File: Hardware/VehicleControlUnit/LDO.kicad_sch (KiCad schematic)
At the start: 5 parts, among them U1 MCP1826S

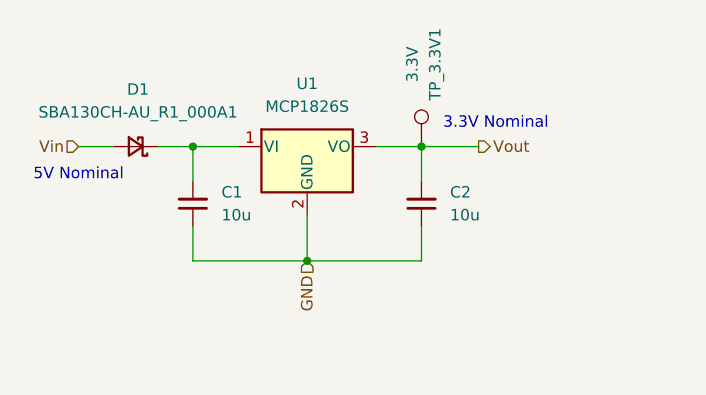
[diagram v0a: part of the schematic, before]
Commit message: mcu pinouts todo - peripherals done
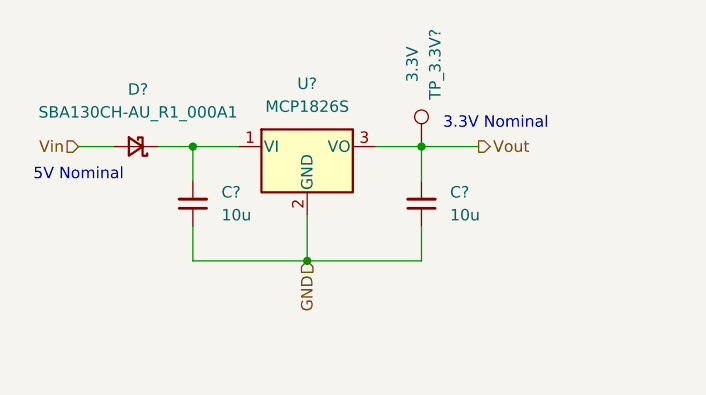
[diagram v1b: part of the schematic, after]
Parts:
- renumbered C2 to C?, C1 to C?, D1 to D?, TP_3.3V1 to TP_3.3V?, U1 to U?
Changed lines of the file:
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@@
 		(dnp no)
 		(fields_autoplaced yes)
-		(property "Reference" "C2"
+		(property "Reference" "C?"
 			(at 168.275 68.5735 0)
 			(show_name no)
@@
 		)
 		(instances
-			(project "LDO"
-				(path "/8ff43370-8d10-4d2c-b1a3-81d1c2934a98"
-					(reference "C2")
-					(unit 1)
-				)
-			)
-			(project "LeaderSOMBreakout"
-				(path "/e5b32072-3e3d-42a6-9d41-1a76d538e329/f3053c74-1ac6-4a33-80f3-565e8c4c2c7d"
+			(project "VehicleControlUnit"
+				(path "/e864fac9-3897-46c9-9101-6d5488c6cd3a/f16a8bc3-f058-4d27-badd-0afc148d009e/da76194f-59e6-4b82-959b-538a81e9eb86"
 					(reference "C?")
-					(unit 1)
-				)
-			)
-			(project "VehicleControlUnit"
-				(path "/e864fac9-3897-46c9-9101-6d5488c6cd3a/3025f6f3-aa95-4f38-bd50-766a08164531"
-					(reference "C2")
 					(unit 1)
 				)
@@
 		(in_pos_files yes)
 		(dnp no)
-		(property "Reference" "TP_3.3V1"
+		(property "Reference" "TP_3.3V?"
 			(at 166.624 54.356 90)
 			(show_name no)
@@
 		)
 		(instances
-			(project "LDO"
-				(path "/8ff43370-8d10-4d2c-b1a3-81d1c2934a98"
-					(reference "TP_3.3V1")
-					(unit 1)
-				)
-			)
 			(project "VehicleControlUnit"
-				(path "/e864fac9-3897-46c9-9101-6d5488c6cd3a/3025f6f3-aa95-4f38-bd50-766a08164531"
-					(reference "TP_3.3V1")
+				(path "/e864fac9-3897-46c9-9101-6d5488c6cd3a/f16a8bc3-f058-4d27-badd-0afc148d009e/da76194f-59e6-4b82-959b-538a81e9eb86"
+					(reference "TP_3.3V?")
 					(unit 1)
 				)
@@
 		(dnp no)
 		(fields_autoplaced yes)
-		(property "Reference" "U1"
+		(property "Reference" "U?"
 			(at 152.4 56.515 0)
 			(show_name no)
@@
 		)
 		(instances
-			(project ""
-				(path "/8ff43370-8d10-4d2c-b1a3-81d1c2934a98"
-					(reference "U1")
-					(unit 1)
-				)
-			)
 			(project "VehicleControlUnit"
-				(path "/e864fac9-3897-46c9-9101-6d5488c6cd3a/3025f6f3-aa95-4f38-bd50-766a08164531"
-					(reference "U1")
+				(path "/e864fac9-3897-46c9-9101-6d5488c6cd3a/f16a8bc3-f058-4d27-badd-0afc148d009e/da76194f-59e6-4b82-959b-538a81e9eb86"
+					(reference "U?")
 					(unit 1)
 				)
@@
 		(dnp no)
 		(fields_autoplaced yes)
-		(property "Reference" "D1"
+		(property "Reference" "D?"
 			(at 133.604 57.15 0)
 			(show_name no)
@@
 		)
 		(instances
-			(project ""
-				(path "/8ff43370-8d10-4d2c-b1a3-81d1c2934a98"
-					(reference "D1")
-					(unit 1)
-				)
-			)
 			(project "VehicleControlUnit"
-				(path "/e864fac9-3897-46c9-9101-6d5488c6cd3a/3025f6f3-aa95-4f38-bd50-766a08164531"
-					(reference "D1")
+				(path "/e864fac9-3897-46c9-9101-6d5488c6cd3a/f16a8bc3-f058-4d27-badd-0afc148d009e/da76194f-59e6-4b82-959b-538a81e9eb86"
+					(reference "D?")
 					(unit 1)
 				)
@@
 		(dnp no)
 		(fields_autoplaced yes)
-		(property "Reference" "C1"
+		(property "Reference" "C?"
 			(at 142.875 68.5735 0)
 			(show_name no)
@@
 		)
 		(instances
-			(project "LDO"
-				(path "/8ff43370-8d10-4d2c-b1a3-81d1c2934a98"
-					(reference "C1")
-					(unit 1)
-				)
-			)
-			(project ""
-				(path "/e5b32072-3e3d-42a6-9d41-1a76d538e329/f3053c74-1ac6-4a33-80f3-565e8c4c2c7d"
+			(project "VehicleControlUnit"
+				(path "/e864fac9-3897-46c9-9101-6d5488c6cd3a/f16a8bc3-f058-4d27-badd-0afc148d009e/da76194f-59e6-4b82-959b-538a81e9eb86"
 					(reference "C?")
 					(unit 1)
 				)
-			)
-			(project "VehicleControlUnit"
-				(path "/e864fac9-3897-46c9-9101-6d5488c6cd3a/3025f6f3-aa95-4f38-bd50-766a08164531"
-					(reference "C1")
-					(unit 1)
-				)

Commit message: VCU more like diddle-u, mika time
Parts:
- gave numbers to parts that had none: 5
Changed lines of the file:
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@@
+		(color 0 0 0 0)
+	)
+	(junction
+		(at 142.24 63.5)
+		(diameter 0)
 		(color 0 0 0 0)
 	)
@@
 	(wire
 		(pts
-			(xy 139.7 63.5) (xy 144.78 63.5)
+			(xy 139.7 63.5) (xy 142.24 63.5)
 		)
 		(stroke
@@
 		(pts
 			(xy 165.1 63.5) (xy 171.45 63.5)
+		)
+		(stroke
+			(width 0)
+			(type default)
+		)
+	)
+	(wire
+		(pts
+			(xy 142.24 63.5) (xy 144.78 63.5)
 		)
 		(stroke
@@
 		(dnp no)
 		(fields_autoplaced yes)
-		(property "Reference" "C?"
+		(property "Reference" "C6"
 			(at 168.275 68.5735 0)
 			(show_name no)
@@
 			(project "VehicleControlUnit"
 				(path "/e864fac9-3897-46c9-9101-6d5488c6cd3a/f16a8bc3-f058-4d27-badd-0afc148d009e/da76194f-59e6-4b82-959b-538a81e9eb86"
-					(reference "C?")
+					(reference "C6")
 					(unit 1)
 				)
@@
 		(in_pos_files yes)
 		(dnp no)
-		(property "Reference" "TP_3.3V?"
+		(property "Reference" "TP_3.3V1"
 			(at 166.624 54.356 90)
 			(show_name no)
@@
 			(project "VehicleControlUnit"
 				(path "/e864fac9-3897-46c9-9101-6d5488c6cd3a/f16a8bc3-f058-4d27-badd-0afc148d009e/da76194f-59e6-4b82-959b-538a81e9eb86"
-					(reference "TP_3.3V?")
+					(reference "TP_3.3V1")
 					(unit 1)
 				)
@@
 		(dnp no)
 		(fields_autoplaced yes)
-		(property "Reference" "U?"
+		(property "Reference" "U2"
 			(at 152.4 56.515 0)
 			(show_name no)
@@
 			(project "VehicleControlUnit"
 				(path "/e864fac9-3897-46c9-9101-6d5488c6cd3a/f16a8bc3-f058-4d27-badd-0afc148d009e/da76194f-59e6-4b82-959b-538a81e9eb86"
-					(reference "U?")
+					(reference "U2")
 					(unit 1)
 				)
@@
 		(dnp no)
 		(fields_autoplaced yes)
-		(property "Reference" "D?"
+		(property "Reference" "D1"
 			(at 133.604 57.15 0)
 			(show_name no)
@@
 			(project "VehicleControlUnit"
 				(path "/e864fac9-3897-46c9-9101-6d5488c6cd3a/f16a8bc3-f058-4d27-badd-0afc148d009e/da76194f-59e6-4b82-959b-538a81e9eb86"
-					(reference "D?")
+					(reference "D1")
+					(unit 1)
+				)
+			)
+		)
+	)
+	(symbol
+		(lib_id "power:PWR_FLAG")
+		(at 142.24 63.5 180)
+		(unit 1)
+		(body_style 1)
+		(exclude_from_sim no)
+		(in_bom yes)
+		(on_board yes)
+		(in_pos_files yes)
+		(dnp no)
+		(fields_autoplaced yes)
+		(property "Reference" "#FLG04"
+			(at 142.24 65.405 0)
+			(hide yes)
+			(show_name no)
+			(do_not_autoplace no)
+			(effects
+				(font
+					(size 1.27 1.27)
+				)
+			)
+		)
+		(property "Value" "PWR_FLAG"
+			(at 142.24 68.58 0)
+			(hide yes)
+			(show_name no)
+			(do_not_autoplace no)
+			(effects
+				(font
+					(size 1.27 1.27)
+				)
+			)
+		)
+		(property "Footprint" ""
+			(at 142.24 63.5 0)
+			(hide yes)
+			(show_name no)
+			(do_not_autoplace no)
+			(effects
+				(font
+					(size 1.27 1.27)
+				)
+			)
+		)
+		(property "Datasheet" ""
+			(at 142.24 63.5 0)
+			(hide yes)
+			(show_name no)
+			(do_not_autoplace no)
+			(effects
+				(font
+					(size 1.27 1.27)
+				)
+			)
+		)
+		(property "Description" "Special symbol for telling ERC where power comes from"
+			(at 142.24 63.5 0)
+			(hide yes)
+			(show_name no)
+			(do_not_autoplace no)
+			(effects
+				(font
+					(size 1.27 1.27)
+				)
+			)
+		)
+		(pin "1"
+		)
+		(instances
+			(project "VehicleControlUnit"
+				(path "/e864fac9-3897-46c9-9101-6d5488c6cd3a/f16a8bc3-f058-4d27-badd-0afc148d009e/da76194f-59e6-4b82-959b-538a81e9eb86"
+					(reference "#FLG04")
 					(unit 1)
 				)
@@
 		(dnp no)
 		(fields_autoplaced yes)
-		(property "Reference" "C?"
+		(property "Reference" "C5"
 			(at 142.875 68.5735 0)
 			(show_name no)
@@
 			(project "VehicleControlUnit"
 				(path "/e864fac9-3897-46c9-9101-6d5488c6cd3a/f16a8bc3-f058-4d27-badd-0afc148d009e/da76194f-59e6-4b82-959b-538a81e9eb86"
-					(reference "C?")
+					(reference "C5")
 					(unit 1)
 				)

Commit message: pre layout
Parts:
- renumbered C5 to C18, C6 to C19, D1 to D3, U2 to U3
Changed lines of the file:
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@@
-		(color 0 0 0 0)
-	)
-	(junction
-		(at 142.24 63.5)
-		(diameter 0)
 		(color 0 0 0 0)
 	)
@@
 	(wire
 		(pts
-			(xy 139.7 63.5) (xy 142.24 63.5)
+			(xy 139.7 63.5) (xy 144.78 63.5)
 		)
 		(stroke
@@
 		(pts
 			(xy 165.1 63.5) (xy 171.45 63.5)
-		)
-		(stroke
-			(width 0)
-			(type default)
-		)
-	)
-	(wire
-		(pts
-			(xy 142.24 63.5) (xy 144.78 63.5)
 		)
 		(stroke
@@
 		(dnp no)
 		(fields_autoplaced yes)
-		(property "Reference" "C6"
+		(property "Reference" "C19"
 			(at 168.275 68.5735 0)
 			(show_name no)
@@
 		)
 		(instances
+			(project "LDO"
+				(path "/8ff43370-8d10-4d2c-b1a3-81d1c2934a98"
+					(reference "C2")
+					(unit 1)
+				)
+			)
+			(project "LeaderSOMBreakout"
+				(path "/e5b32072-3e3d-42a6-9d41-1a76d538e329/f3053c74-1ac6-4a33-80f3-565e8c4c2c7d"
+					(reference "C?")
+					(unit 1)
+				)
+			)
 			(project "VehicleControlUnit"
-				(path "/e864fac9-3897-46c9-9101-6d5488c6cd3a/f16a8bc3-f058-4d27-badd-0afc148d009e/da76194f-59e6-4b82-959b-538a81e9eb86"
-					(reference "C6")
+				(path "/e864fac9-3897-46c9-9101-6d5488c6cd3a/f16a8bc3-f058-4d27-badd-0afc148d009e/853b16d2-2efa-4055-8a9a-ea208220d84d"
+					(reference "C19")
 					(unit 1)
 				)
@@
 		)
 		(instances
+			(project "LDO"
+				(path "/8ff43370-8d10-4d2c-b1a3-81d1c2934a98"
+					(reference "TP_3.3V1")
+					(unit 1)
+				)
+			)
 			(project "VehicleControlUnit"
-				(path "/e864fac9-3897-46c9-9101-6d5488c6cd3a/f16a8bc3-f058-4d27-badd-0afc148d009e/da76194f-59e6-4b82-959b-538a81e9eb86"
+				(path "/e864fac9-3897-46c9-9101-6d5488c6cd3a/f16a8bc3-f058-4d27-badd-0afc148d009e/853b16d2-2efa-4055-8a9a-ea208220d84d"
 					(reference "TP_3.3V1")
 					(unit 1)
@@
 		(dnp no)
 		(fields_autoplaced yes)
-		(property "Reference" "U2"
+		(property "Reference" "U3"
 			(at 152.4 56.515 0)
 			(show_name no)
@@
 		)
 		(instances
+			(project ""
+				(path "/8ff43370-8d10-4d2c-b1a3-81d1c2934a98"
+					(reference "U1")
+					(unit 1)
+				)
+			)
 			(project "VehicleControlUnit"
-				(path "/e864fac9-3897-46c9-9101-6d5488c6cd3a/f16a8bc3-f058-4d27-badd-0afc148d009e/da76194f-59e6-4b82-959b-538a81e9eb86"
-					(reference "U2")
+				(path "/e864fac9-3897-46c9-9101-6d5488c6cd3a/f16a8bc3-f058-4d27-badd-0afc148d009e/853b16d2-2efa-4055-8a9a-ea208220d84d"
+					(reference "U3")
 					(unit 1)
 				)
@@
 		(dnp no)
 		(fields_autoplaced yes)
-		(property "Reference" "D1"
+		(property "Reference" "D3"
 			(at 133.604 57.15 0)
 			(show_name no)
@@
 		)
 		(instances
-			(project "VehicleControlUnit"
-				(path "/e864fac9-3897-46c9-9101-6d5488c6cd3a/f16a8bc3-f058-4d27-badd-0afc148d009e/da76194f-59e6-4b82-959b-538a81e9eb86"
+			(project ""
+				(path "/8ff43370-8d10-4d2c-b1a3-81d1c2934a98"
 					(reference "D1")
 					(unit 1)
 				)
 			)
-		)
-	)
-	(symbol
-		(lib_id "power:PWR_FLAG")
-		(at 142.24 63.5 180)
-		(unit 1)
-		(body_style 1)
-		(exclude_from_sim no)
-		(in_bom yes)
-		(on_board yes)
-		(in_pos_files yes)
-		(dnp no)
-		(fields_autoplaced yes)
-		(property "Reference" "#FLG08"
-			(at 142.24 65.405 0)
-			(hide yes)
-			(show_name no)
-			(do_not_autoplace no)
-			(effects
-				(font
-					(size 1.27 1.27)
-				)
-			)
-		)
-		(property "Value" "PWR_FLAG"
-			(at 142.24 68.58 0)
-			(hide yes)
-			(show_name no)
-			(do_not_autoplace no)
-			(effects
-				(font
-					(size 1.27 1.27)
-				)
-			)
-		)
-		(property "Footprint" ""
-			(at 142.24 63.5 0)
-			(hide yes)
-			(show_name no)
-			(do_not_autoplace no)
-			(effects
-				(font
-					(size 1.27 1.27)
-				)
-			)
-		)
-		(property "Datasheet" ""
-			(at 142.24 63.5 0)
-			(hide yes)
-			(show_name no)
-			(do_not_autoplace no)
-			(effects
-				(font
-					(size 1.27 1.27)
-				)
-			)
-		)
-		(property "Description" "Special symbol for telling ERC where power comes from"
-			(at 142.24 63.5 0)
-			(hide yes)
-			(show_name no)
-			(do_not_autoplace no)
-			(effects
-				(font
-					(size 1.27 1.27)
-				)
-			)
-		)
-		(pin "1"
-		)
-		(instances
 			(project "VehicleControlUnit"
-				(path "/e864fac9-3897-46c9-9101-6d5488c6cd3a/f16a8bc3-f058-4d27-badd-0afc148d009e/da76194f-59e6-4b82-959b-538a81e9eb86"
-					(reference "#FLG08")
+				(path "/e864fac9-3897-46c9-9101-6d5488c6cd3a/f16a8bc3-f058-4d27-badd-0afc148d009e/853b16d2-2efa-4055-8a9a-ea208220d84d"
+					(reference "D3")
 					(unit 1)
 				)
@@
 		(dnp no)
 		(fields_autoplaced yes)
-		(property "Reference" "C5"
+		(property "Reference" "C18"
 			(at 142.875 68.5735 0)
 			(show_name no)
@@
 		)
 		(instances
+			(project "LDO"
+				(path "/8ff43370-8d10-4d2c-b1a3-81d1c2934a98"
+					(reference "C1")
+					(unit 1)
+				)
+			)
+			(project ""
+				(path "/e5b32072-3e3d-42a6-9d41-1a76d538e329/f3053c74-1ac6-4a33-80f3-565e8c4c2c7d"
+					(reference "C?")
+					(unit 1)
+				)
+			)
 			(project "VehicleControlUnit"
-				(path "/e864fac9-3897-46c9-9101-6d5488c6cd3a/f16a8bc3-f058-4d27-badd-0afc148d009e/da76194f-59e6-4b82-959b-538a81e9eb86"
-					(reference "C5")
+				(path "/e864fac9-3897-46c9-9101-6d5488c6cd3a/f16a8bc3-f058-4d27-badd-0afc148d009e/853b16d2-2efa-4055-8a9a-ea208220d84d"
+					(reference "C18")
 					(unit 1)
 				)
